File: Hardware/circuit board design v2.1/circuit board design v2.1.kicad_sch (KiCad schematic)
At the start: 0 parts

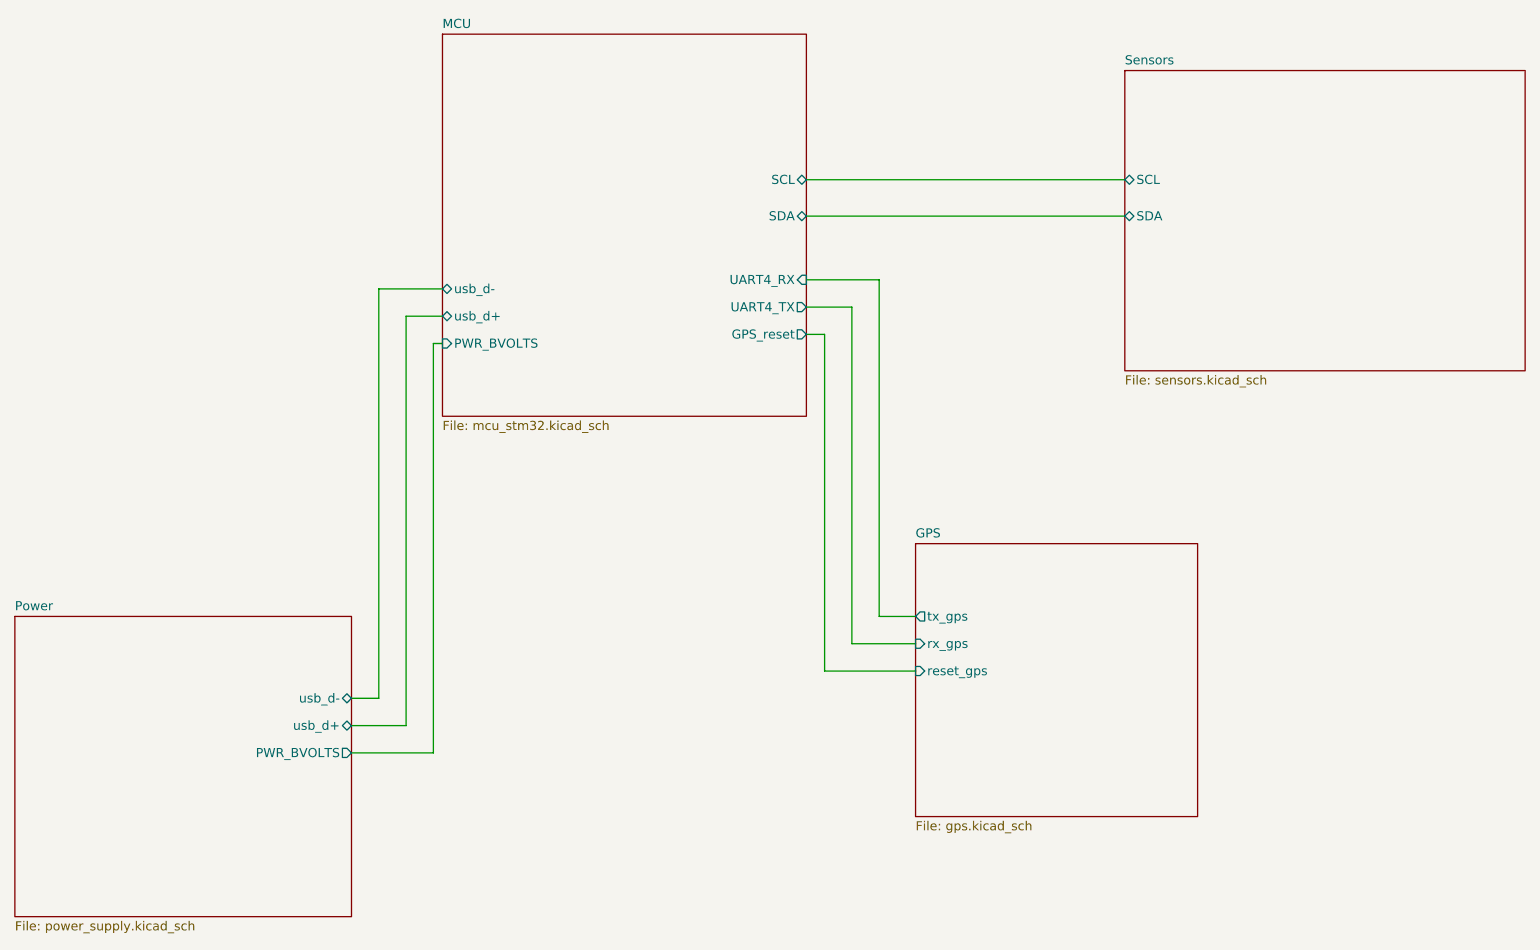
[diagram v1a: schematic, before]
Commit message: Renamed pins in stm32cubeide and finished routing for V2.1
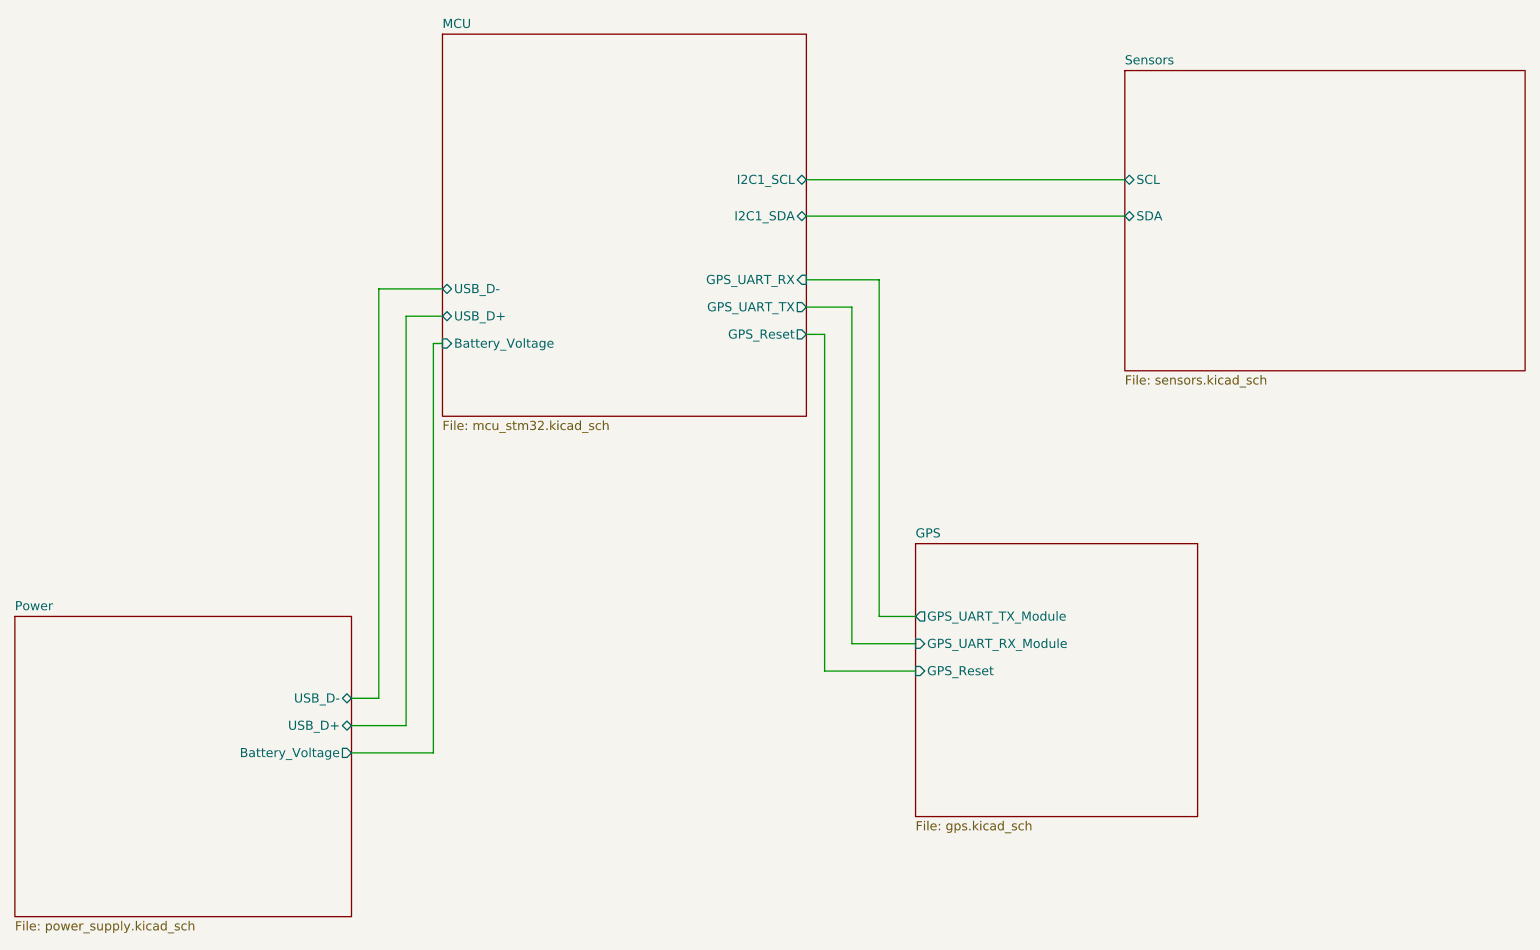
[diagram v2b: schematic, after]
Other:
- sheet GPS ports: added GPS_Reset, GPS_UART_RX_Module, GPS_UART_TX_Module; removed reset_gps, rx_gps, tx_gps
- sheet MCU ports: added Battery_Voltage, GPS_Reset, GPS_UART_RX, GPS_UART_TX, I2C1_SCL, I2C1_SDA, USB_D+, USB_D-; removed GPS_reset, PWR_BVOLTS, SCL, SDA, UART4_RX, UART4_TX, usb_d+, usb_d-
- sheet Power ports: added Battery_Voltage, USB_D+, USB_D-; removed PWR_BVOLTS, usb_d+, usb_d-
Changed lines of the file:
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@@
       (effects (font (size 1.27 1.27)) (justify left top))
     )
-    (pin "PWR_BVOLTS" output (at 78.74 133.35 0)
-      (effects (font (size 1.27 1.27)) (justify right))
-    )
-    (pin "usb_d+" bidirectional (at 78.74 129.54 0)
-      (effects (font (size 1.27 1.27)) (justify right))
-    )
-    (pin "usb_d-" bidirectional (at 78.74 125.73 0)
+    (pin "Battery_Voltage" output (at 78.74 133.35 0)
+      (effects (font (size 1.27 1.27)) (justify right))
+    )
+    (pin "USB_D+" bidirectional (at 78.74 129.54 0)
+      (effects (font (size 1.27 1.27)) (justify right))
+    )
+    (pin "USB_D-" bidirectional (at 78.74 125.73 0)
       (effects (font (size 1.27 1.27)) (justify right))
     )
@@
       (effects (font (size 1.27 1.27)) (justify left top))
     )
-    (pin "rx_gps" input (at 157.48 118.11 180)
-      (effects (font (size 1.27 1.27)) (justify left))
-    )
-    (pin "tx_gps" output (at 157.48 114.3 180)
-      (effects (font (size 1.27 1.27)) (justify left))
-    )
-    (pin "reset_gps" input (at 157.48 121.92 180)
+    (pin "GPS_Reset" input (at 157.48 121.92 180)
+      (effects (font (size 1.27 1.27)) (justify left))
+    )
+    (pin "GPS_UART_TX_Module" output (at 157.48 114.3 180)
+      (effects (font (size 1.27 1.27)) (justify left))
+    )
+    (pin "GPS_UART_RX_Module" input (at 157.48 118.11 180)
       (effects (font (size 1.27 1.27)) (justify left))
     )
@@
       (effects (font (size 1.27 1.27)) (justify left top))
     )
-    (pin "SDA" bidirectional (at 142.24 58.42 0)
-      (effects (font (size 1.27 1.27)) (justify right))
-    )
-    (pin "SCL" bidirectional (at 142.24 53.34 0)
-      (effects (font (size 1.27 1.27)) (justify right))
-    )
-    (pin "UART4_RX" input (at 142.24 67.31 0)
-      (effects (font (size 1.27 1.27)) (justify right))
-    )
-    (pin "UART4_TX" output (at 142.24 71.12 0)
-      (effects (font (size 1.27 1.27)) (justify right))
-    )
-    (pin "PWR_BVOLTS" input (at 91.44 76.2 180)
-      (effects (font (size 1.27 1.27)) (justify left))
-    )
-    (pin "usb_d-" bidirectional (at 91.44 68.58 180)
-      (effects (font (size 1.27 1.27)) (justify left))
-    )
-    (pin "usb_d+" bidirectional (at 91.44 72.39 180)
-      (effects (font (size 1.27 1.27)) (justify left))
-    )
-    (pin "GPS_reset" output (at 142.24 74.93 0)
+    (pin "Battery_Voltage" input (at 91.44 76.2 180)
+      (effects (font (size 1.27 1.27)) (justify left))
+    )
+    (pin "GPS_UART_RX" input (at 142.24 67.31 0)
+      (effects (font (size 1.27 1.27)) (justify right))
+    )
+    (pin "GPS_UART_TX" output (at 142.24 71.12 0)
+      (effects (font (size 1.27 1.27)) (justify right))
+    )
+    (pin "GPS_Reset" output (at 142.24 74.93 0)
+      (effects (font (size 1.27 1.27)) (justify right))
+    )
+    (pin "USB_D-" bidirectional (at 91.44 68.58 180)
+      (effects (font (size 1.27 1.27)) (justify left))
+    )
+    (pin "USB_D+" bidirectional (at 91.44 72.39 180)
+      (effects (font (size 1.27 1.27)) (justify left))
+    )
+    (pin "I2C1_SDA" bidirectional (at 142.24 58.42 0)
+      (effects (font (size 1.27 1.27)) (justify right))
+    )
+    (pin "I2C1_SCL" bidirectional (at 142.24 53.34 0)
       (effects (font (size 1.27 1.27)) (justify right))
     )
@@
     )
     (path "/b2e7fea0-7ba9-48b0-990f-5c369d704fdf/d11c8c2e-e9f5-485e-999a-64fceff9aa62"
-      (reference "R3") (unit 1) (value "R_0603") (footprint "Components:R_0603_1608Metric")
+      (reference "R3") (unit 1) (value "330") (footprint "Components:R_0603_1608Metric")
     )
     (path "/b2e7fea0-7ba9-48b0-990f-5c369d704fdf/a6e9bac5-48c4-4743-ae7b-3db6d10615a6"
-      (reference "R4") (unit 1) (value "R_0603") (footprint "Components:R_0603_1608Metric")
+      (reference "R4") (unit 1) (value "330") (footprint "Components:R_0603_1608Metric")
     )
     (path "/91cf0010-9ee0-4eb5-a57e-e0ac00755c97/df6bec52-9ff5-48f0-90ca-2b54ce92b35c"
